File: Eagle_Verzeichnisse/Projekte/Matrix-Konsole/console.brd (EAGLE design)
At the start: 200.6 x 200.3 mm, 15 parts, among them J1 DIN5, J2 DIN5, J3 DIN5, J4 DIN5, X2 057-016-1

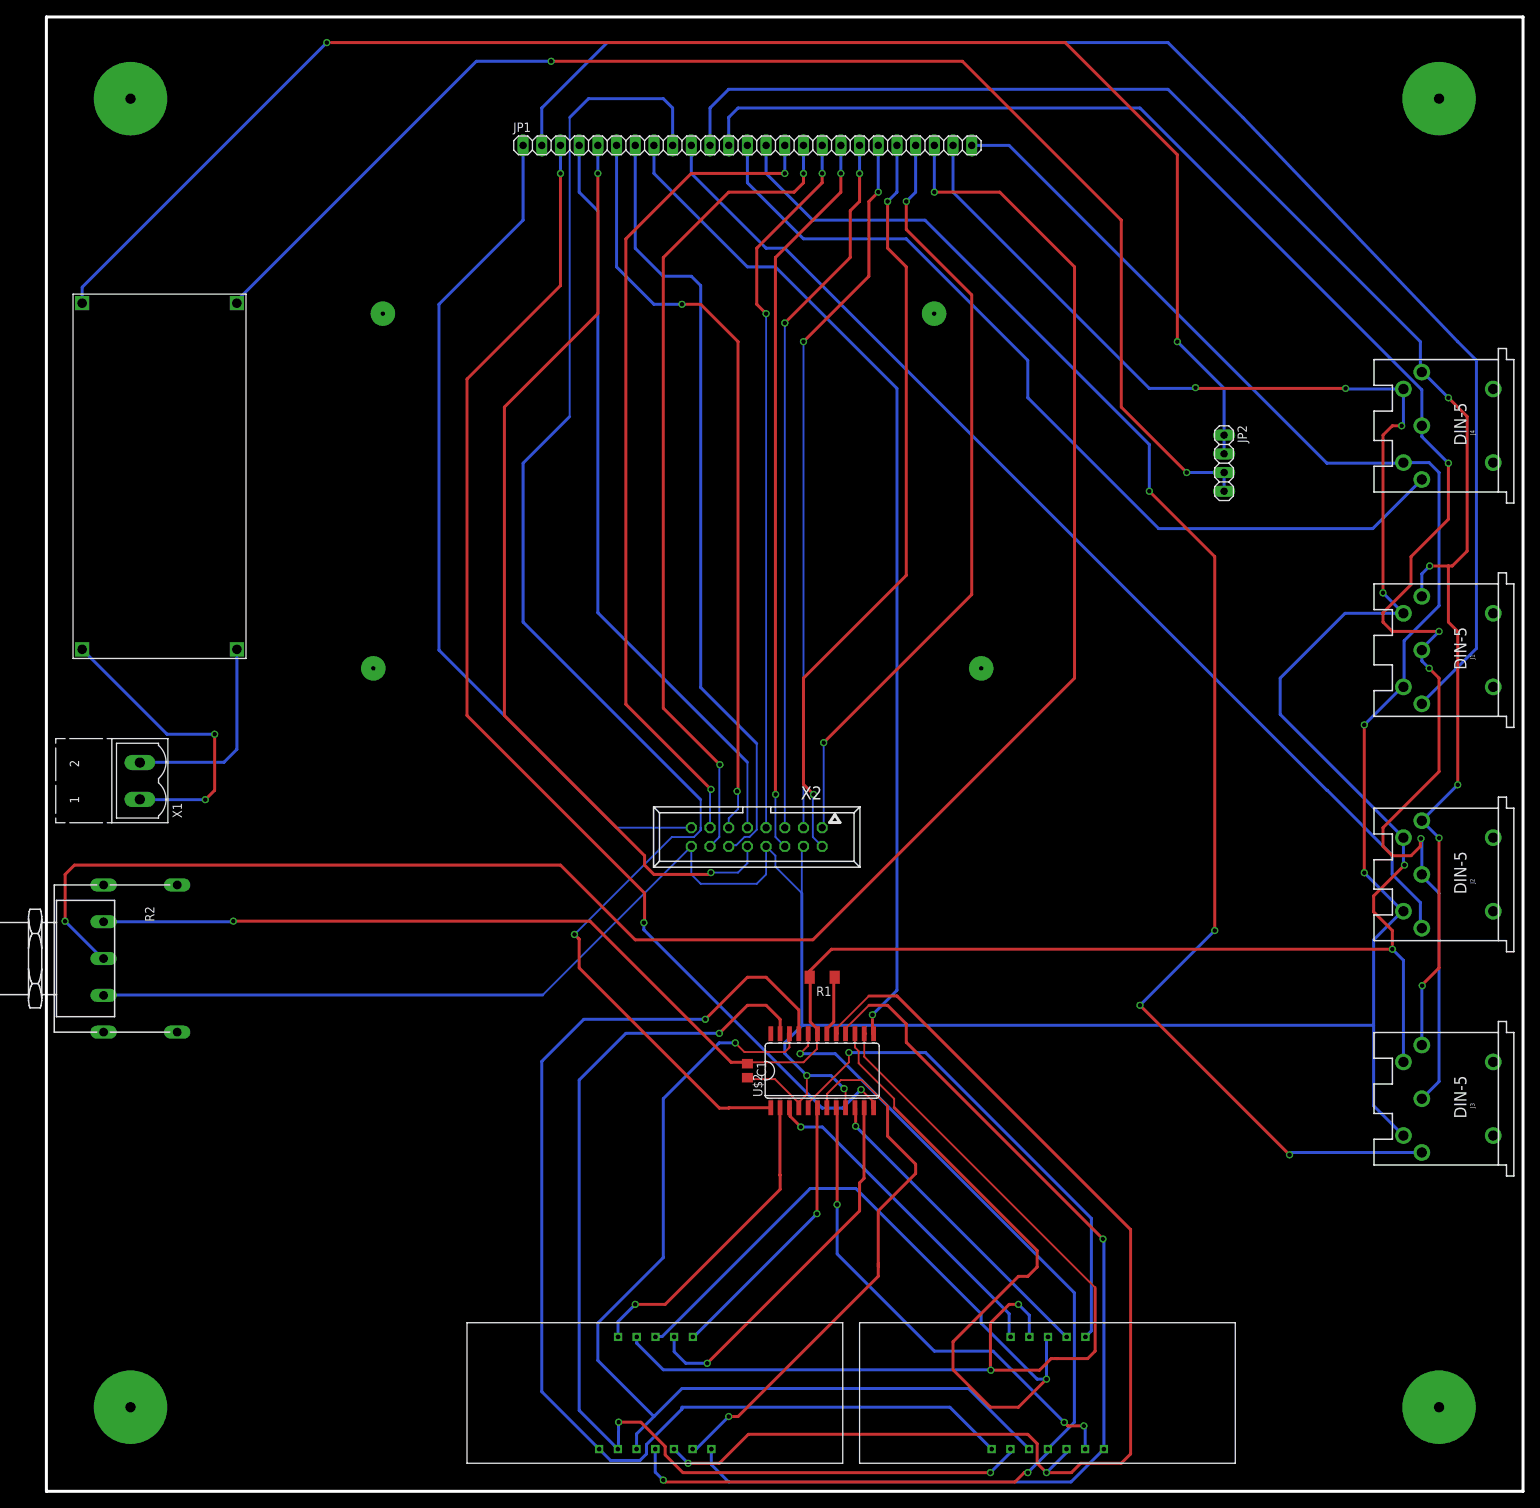
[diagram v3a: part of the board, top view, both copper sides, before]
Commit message: Added controller-layout, Improved console-layout
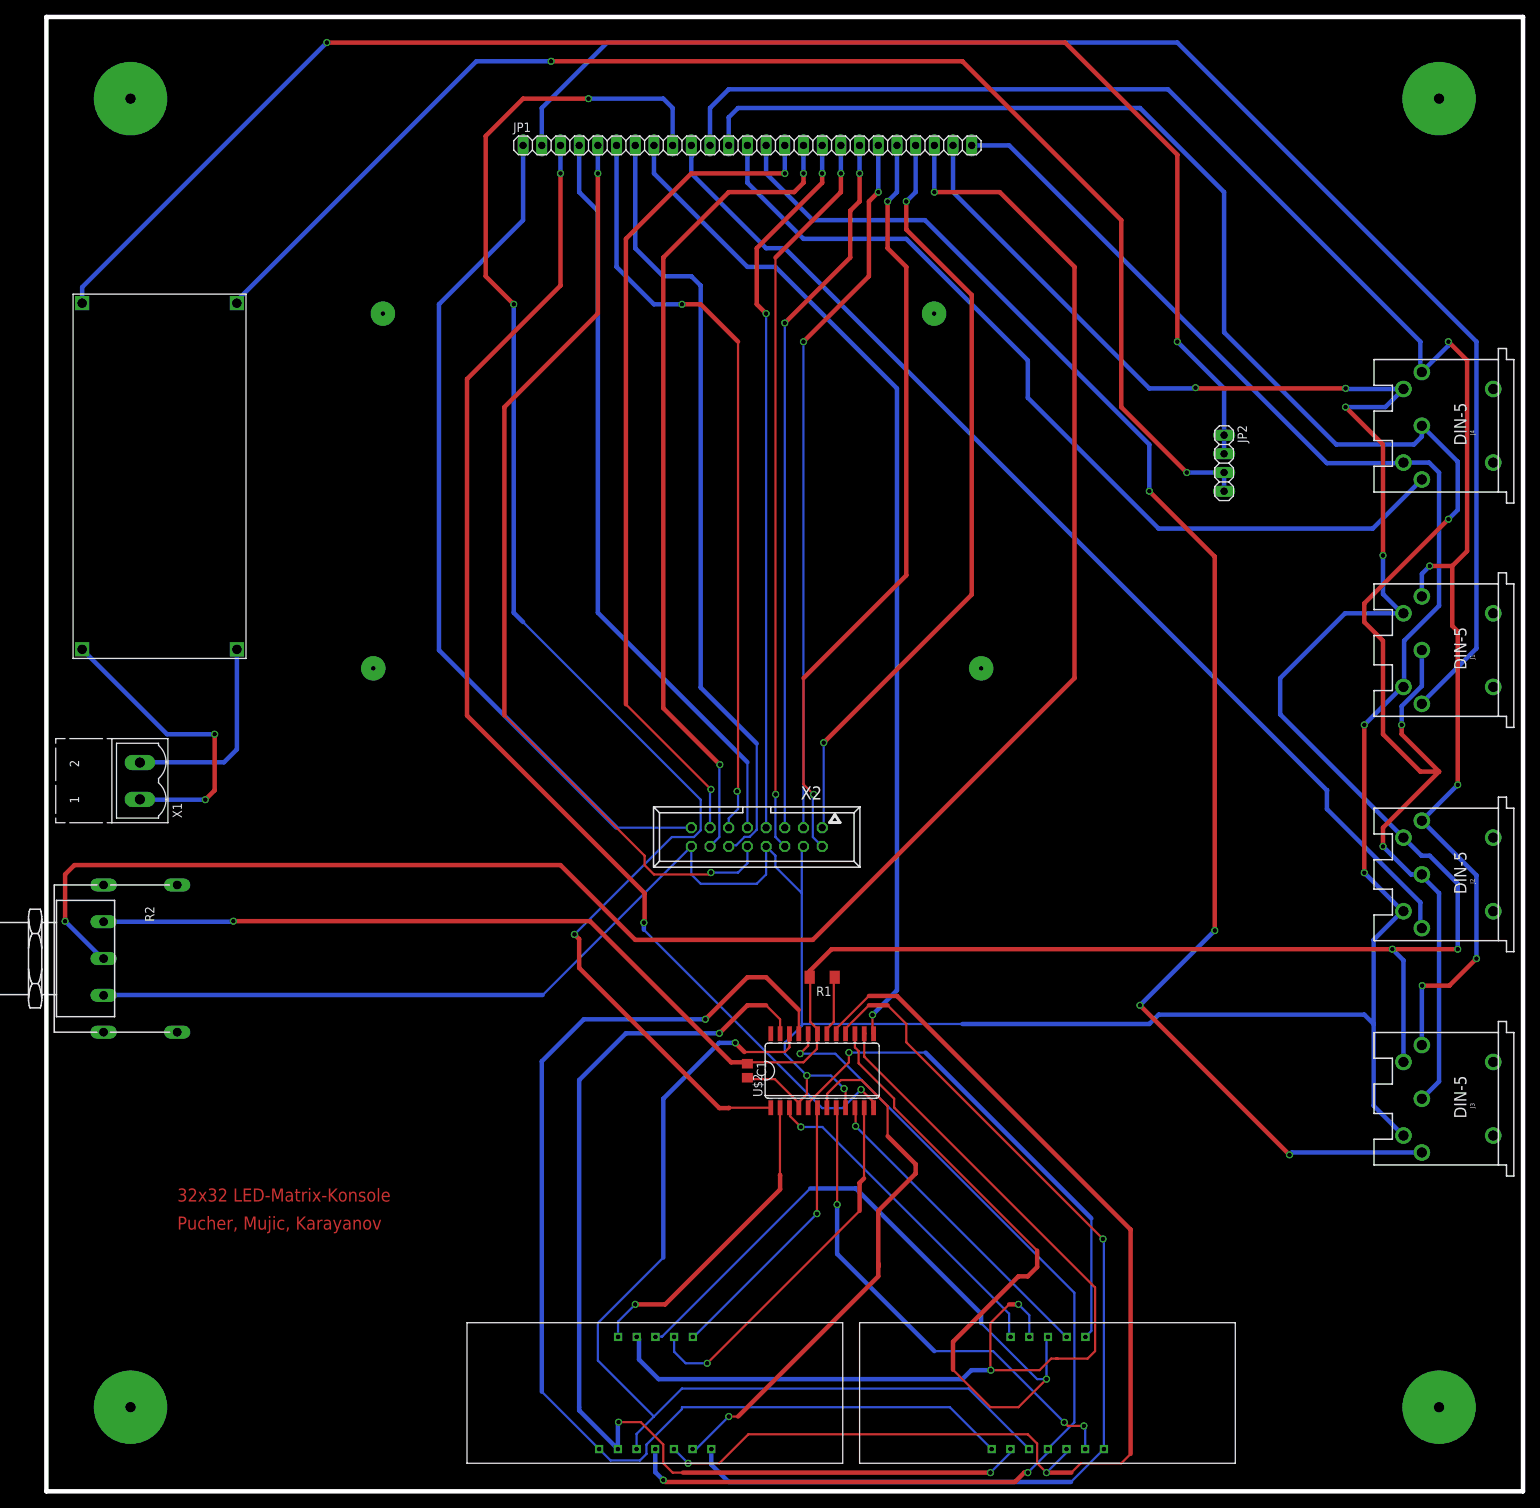
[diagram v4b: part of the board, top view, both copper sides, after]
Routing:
- net CLK: track 238.8 -> 263.2 mm, vias 4 -> 3
- net 5V: track 393.8 -> 410.3 mm
- net PL: track 228.3 -> 242.6 mm
- net MAX_DIN: track 192.2 -> 201.4 mm, vias 1 -> 3
- net A: track 138.8 -> 141.3 mm
- net SER4: track 203.9 -> 205.0 mm
- net MEGA_GND: track 431.8 -> 433.0 mm
- net D: track 149.3 -> 150.2 mm
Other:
- board text added: "32x32 LED-Matrix-Konsole"
- board text added: "Pucher, Mujic, Karayanov"

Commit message: Improved layouts
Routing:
- net D: track 150.2 -> 204.5 mm
- net F: track 156.7 -> 192.6 mm
- net A: track 141.3 -> 129.7 mm, vias 2 -> 1
- net MEGA_GND: track 433.0 -> 431.7 mm

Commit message: Splitted the console-layout into three boards and improved the layouts
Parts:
- removed 7SEG1, 7SEG2: 7SEG_DEV, seven_segment:7SEG_PACK
- removed C1: 100n, eagle-ltspice:C0805
- removed J1, J2, J3, J4: DIN5, SparkFun-Connectors:DIN5-RA-PTH
- removed R1: 200, resistor:M3516
- removed U$2: MAX7219CWG, max7219:SO24L
- added JP3: (no value), pinhead:1X05
- added JP4: (no value), pinhead:1X04
- JP2: device pinhead:1X04 -> pinhead:1X08
- moved JP1 146.0 mm to (61.0, 40.6), turned to 180 degrees
- moved JP2 103.6 mm to (129.5, 40.6), turned to 180 degrees
- moved U$1 81.2 mm to (45.7, 62.2), turned to 0 degrees
- moved X2 36.9 mm to (113.0, 55.9)
- moved X1 29.0 mm to (5.08, 68.6), turned to 270 degrees
- moved R2 25.4 mm to (1.27, 47.0)
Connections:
- removed net A: 7SEG1.11, 7SEG2.11, U$2.14
- removed net B: 7SEG1.7, 7SEG2.7, U$2.16
- removed net C: 7SEG1.4, 7SEG2.4, U$2.20
- removed net D: 7SEG1.2, 7SEG2.2, U$2.23
- removed net DIG0: 7SEG1.12, U$2.2
- removed net DIG1: 7SEG1.9, U$2.11
- removed net DIG2: 7SEG1.8, U$2.6
- removed net DIG3: 7SEG1.6, U$2.7
- removed net DIG4: 7SEG2.12, U$2.3
- removed net DIG5: 7SEG2.9, U$2.10
- removed net DIG6: 7SEG2.8, U$2.5
- removed net DIG7: 7SEG2.6, U$2.8
- removed net DP: 7SEG1.3, 7SEG2.3, U$2.22
- removed net E: 7SEG1.1, 7SEG2.1, U$2.21
- removed net F: 7SEG1.10, 7SEG2.10, U$2.15
- removed net G: 7SEG1.5, 7SEG2.5, U$2.17
- removed net MAX_ISET: R1.1, U$2.18
- removed net N$1: JP2.1, JP2.2, U$1.OUT+
- removed net N$8: JP2.3, JP2.4, U$1.OUT-
- new net MATRIX_GND: JP4.4, U$1.OUT-
- new net MATRIX_VCC: JP4.1, U$1.OUT+
- net 5V: now also JP2.1, JP3.1; no longer C1.1, J1.4, J2.4, J3.4, J4.4, R1.2, U$2.19
- net CLK: now also JP2.3; no longer J1.2, J2.2, J3.2, J4.2
- net MAX_CLK: now also JP3.3; no longer U$2.13
- net MAX_DIN: now also JP3.5; no longer U$2.1
- net MAX_LOAD: now also JP3.4; no longer U$2.12
- net MEGA_GND: now also JP2.2, JP3.2; no longer C1.2, J1.5, J2.5, J3.5, J4.5, U$2.4, U$2.9
- net PL: now also JP2.4; no longer J1.1, J2.1, J3.1, J4.1
- net SER1: now also JP2.8; no longer J4.3
- net SER2: now also JP2.7; no longer J3.3
- net SER3: now also JP2.6; no longer J2.3
- net SER4: now also JP2.5; no longer J1.3
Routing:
- net 5V: track 410.3 -> 174.7 mm, vias 7 -> 2
- net N$1: track 214.3 -> 0.00 mm, vias 2 -> 0
- net MEGA_A9: track 255.8 -> 47.2 mm, vias 2 -> 0
- net D: track 204.5 -> 0.00 mm, vias 3 -> 0
- net F: track 192.6 -> 0.00 mm, vias 1 -> 0
- net MEGA_GND: track 431.7 -> 241.6 mm, vias 4 -> 0
- net N$8: track 188.5 -> 0.00 mm, vias 2 -> 0
- net MATRIX_OE: track 117.8 -> 282.4 mm, vias 0 -> 2
- net MATRIX_A: track 102.2 -> 265.3 mm, vias 0 -> 2
- net E: track 161.9 -> 0.00 mm, vias 1 -> 0
- net G: track 160.6 -> 0.00 mm, vias 2 -> 0
- net CLK: track 263.2 -> 106.0 mm, vias 3 -> 2
- net B: track 138.5 -> 0.00 mm, vias 1 -> 0
- net MAX_DIN: track 201.4 -> 63.8 mm, vias 3 -> 2
- net C: track 135.8 -> 0.00 mm, vias 3 -> 0
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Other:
- board size 200.6 x 200.3 mm -> 143.5 x 83.5 mm
- board text added: "LED-Matrix-Konsole Karayanov, Mujic, Pucher"
- board text removed: "32x32 LED-Matrix-Konsole"
- board text removed: "Pucher, Mujic, Karayanov"

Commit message: Made final changes to the layout and added PDF-Files
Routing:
- net N$1: track 0.00 -> 454.7 mm
- net 5V: track 174.7 -> 164.4 mm
- net MATRIX_A: track 265.3 -> 272.1 mm
- net MATRIX_B: track 241.6 -> 247.5 mm
- net MEGA_A9: track 47.2 -> 52.3 mm
- net SER3: track 110.9 -> 107.2 mm
- net MATRIX_C: track 213.3 -> 209.7 mm
- net MATRIX_B2: track 194.6 -> 197.7 mm
- net PL: track 116.0 -> 113.2 mm
- net SER1: track 94.0 -> 95.4 mm
- net MATRIX_CLK: track 167.6 -> 166.5 mm
- net MAX_LOAD: track 45.9 -> 46.6 mm
- net SER4: track 91.3 -> 92.1 mm
- net MATRIX_D: track 52.6 -> 53.4 mm
- net MATRIX_LAT: track 166.4 -> 167.0 mm
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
